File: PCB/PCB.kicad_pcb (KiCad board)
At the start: 2 copper layers, 64.8 x 61 mm, 54 parts, among them J2 Conn_01x02_Pin, J3 Conn_01x02_Pin, J5 Conn_01x04_Pin, SW1 SW_Push, U1 STM32L476RGTx, U2 FGPMMOPA6H, U4 TPS63001DRCR, U5 LM2735XMF/NOPB, U8 LM386, U9 MAX7375AXR805

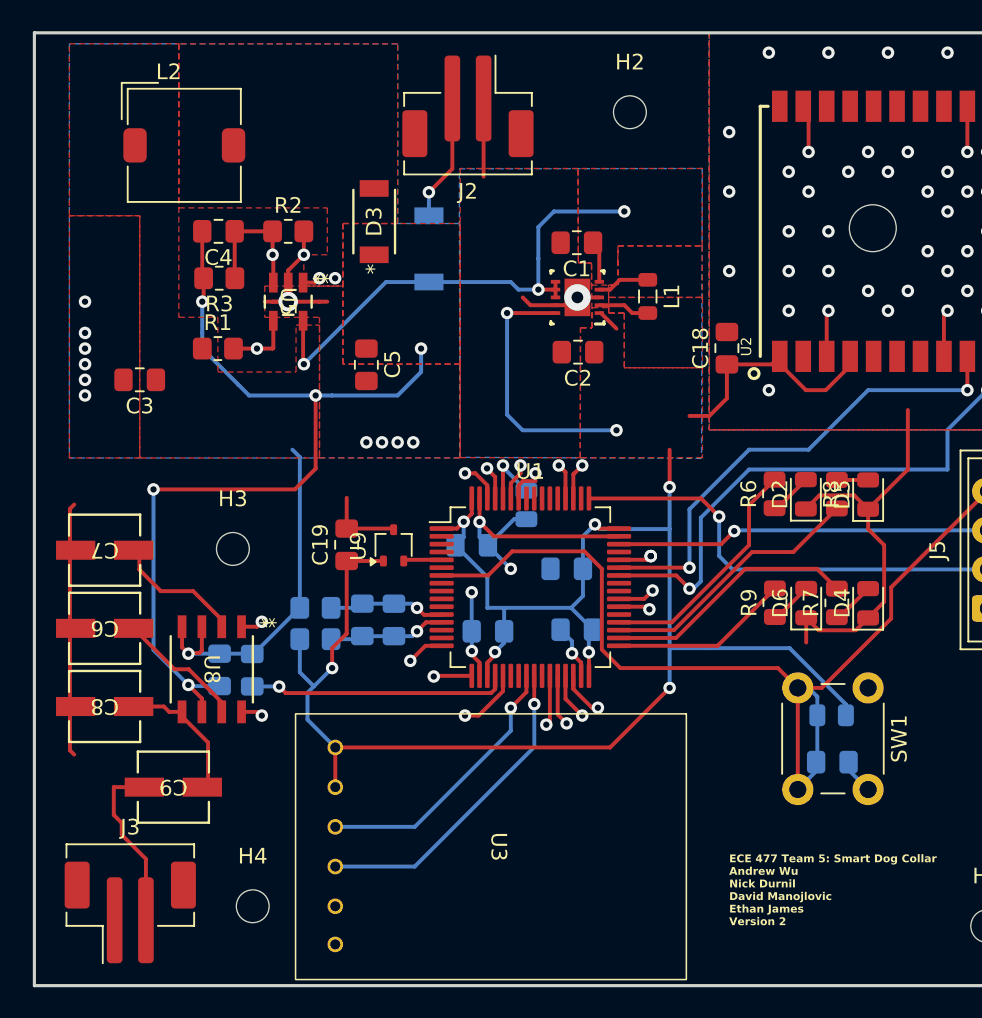
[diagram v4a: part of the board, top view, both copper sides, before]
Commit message: silkscreen visibility fix
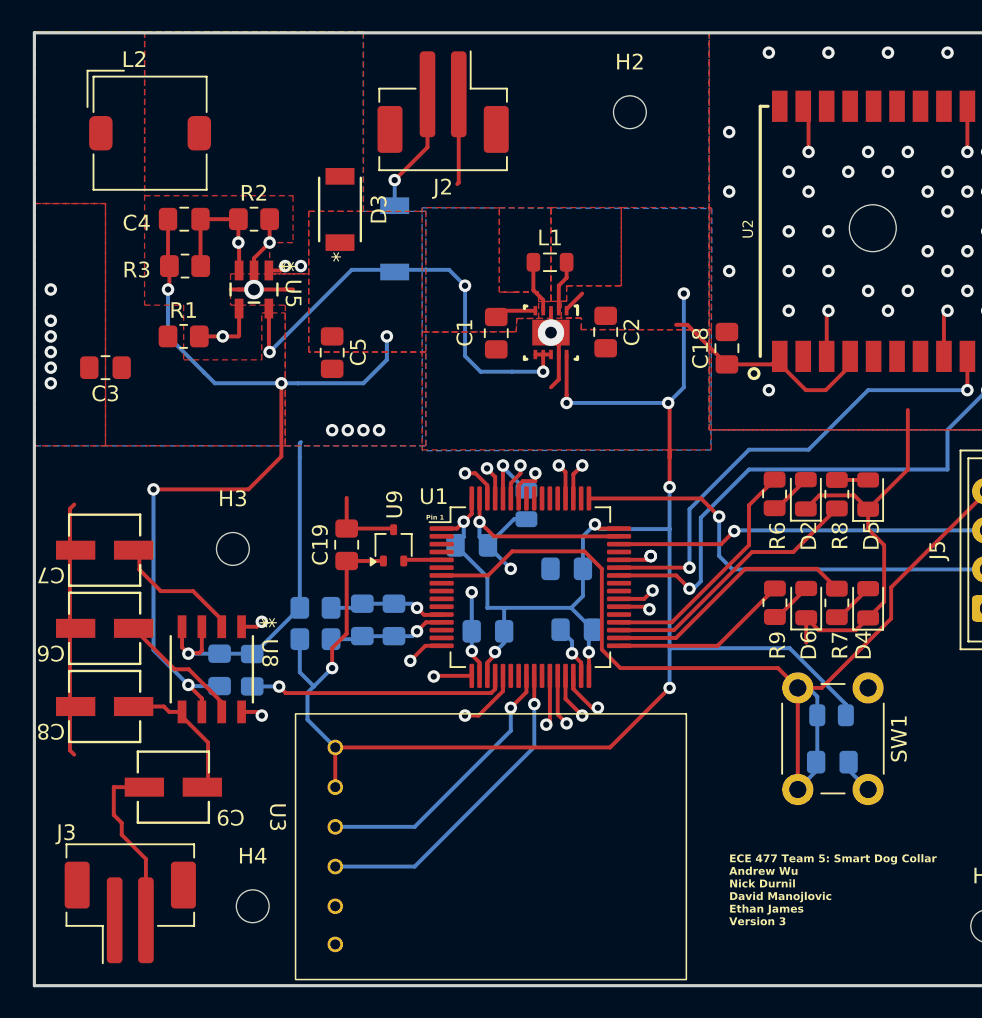
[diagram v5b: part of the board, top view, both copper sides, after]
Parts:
- moved C1 7.75 mm to (201.0, 103.0), turned to -90 degrees
- moved L1 6.63 mm to (204.4, 98.5), turned to 0 degrees
- moved U4 2.82 mm to (204.5, 103.0), turned to -90 degrees
- moved C3 2.32 mm to (176.0, 105.2)
- moved C4 2.32 mm to (181.0, 95.7)
- moved C5 2.32 mm to (190.5, 104.3)
- moved D3 2.32 mm to (191.0, 95.1)
- moved L2 2.32 mm to (178.8, 90.2)
- moved R1 2.32 mm to (181.0, 103.2)
- moved R2 2.32 mm to (185.5, 95.7)
- moved R3 2.32 mm to (181.1, 98.7)
- moved U5 2.32 mm to (185.5, 100.2)
- moved D1 2.28 mm to (194.5, 97.0)
- moved C2 2.19 mm to (208.0, 103.0), turned to -90 degrees
- moved J2 1.61 mm to (197.6, 88.2)
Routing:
- net +3.3V: track 145.3 -> 148.1 mm, vias 9 -> 10
- net /Bat +: track 34.9 -> 32.6 mm
- net +5V: track 58.1 -> 56.2 mm
- net GND: track 132.9 -> 134.0 mm
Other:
- board text added: "ECE 477 Team 5: Smart Dog Collar Andrew Wu Nick Durnil David Manojlovic Ethan James Version 3"
- board text added: "Pin 1"
- board text removed: "ECE 477 Team 5: Smart Dog Collar Andrew Wu Nick Durnil David Manojlovic Ethan James Version 2"

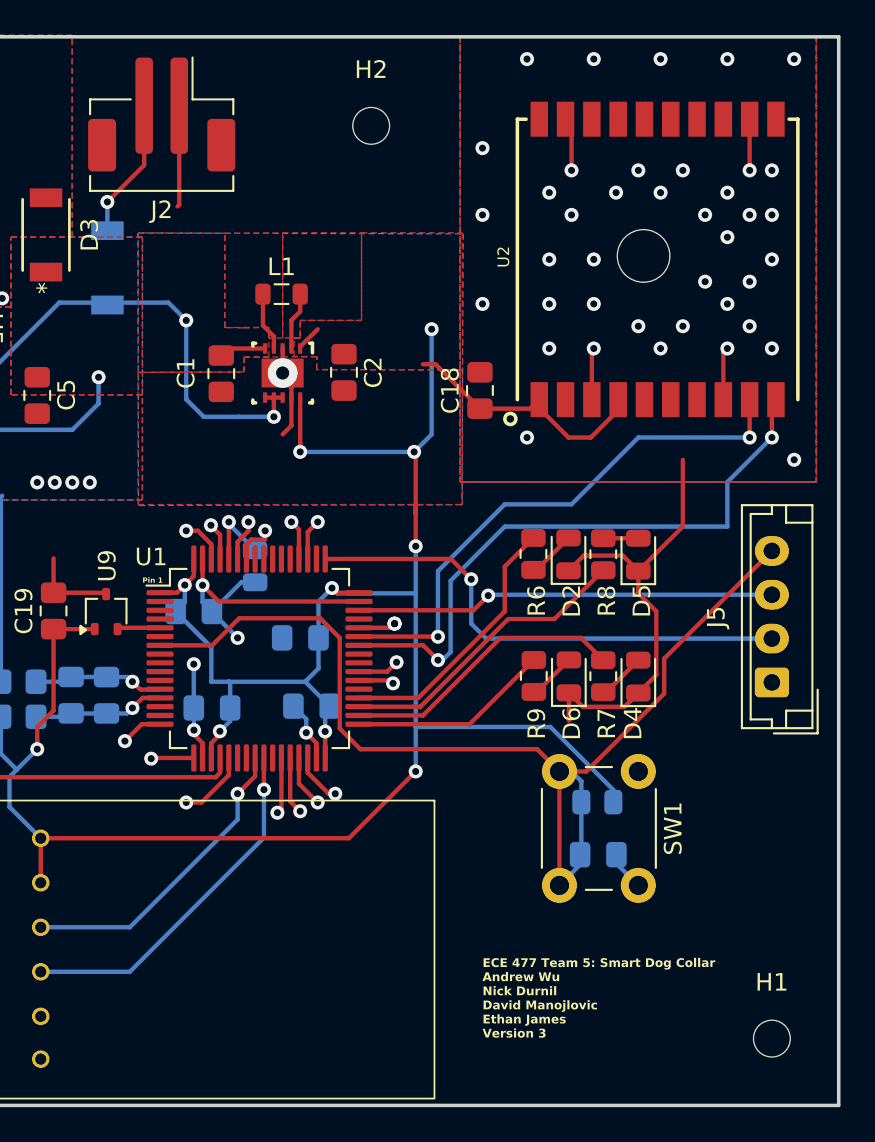
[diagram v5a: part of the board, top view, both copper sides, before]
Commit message: tweaks based on email
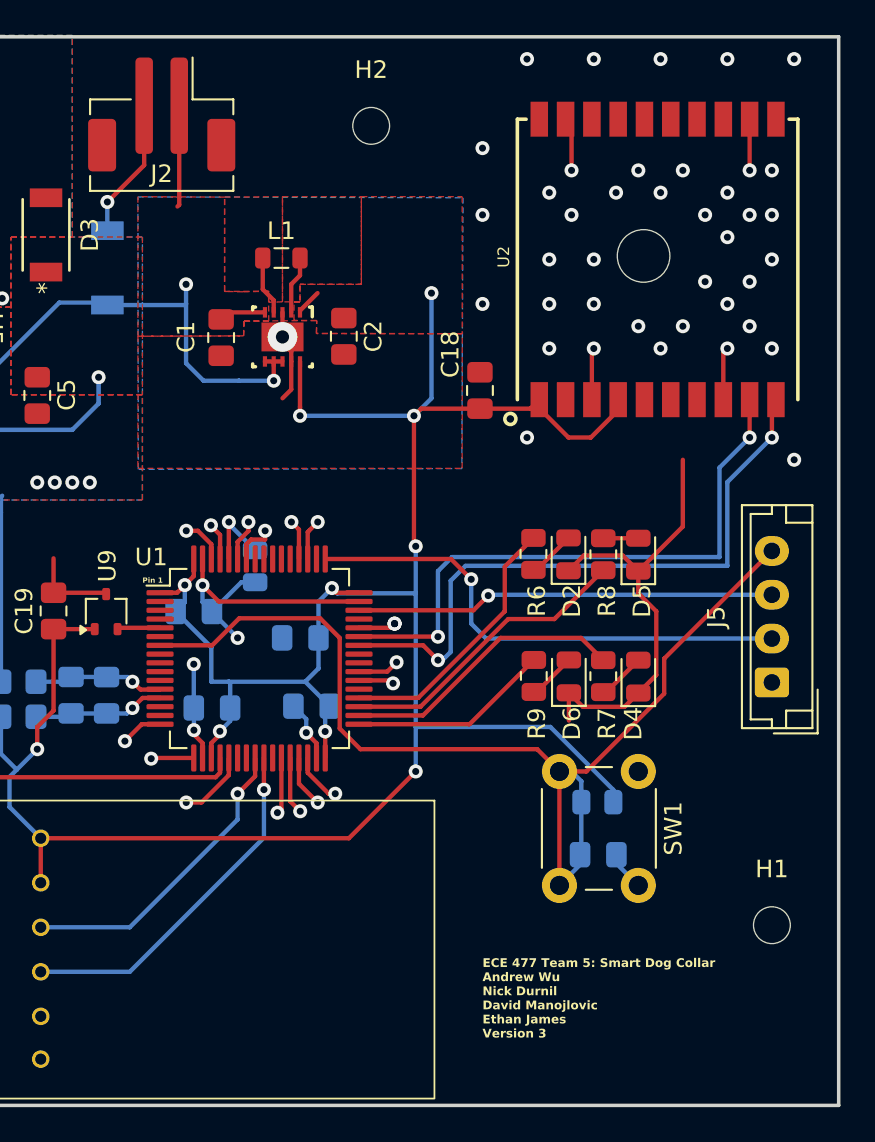
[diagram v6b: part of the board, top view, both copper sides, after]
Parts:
- moved H1 6.47 mm to (232.4, 134.5)
- moved C1 2.06 mm to (201.0, 101.0)
- moved C2 2.06 mm to (208.0, 100.9)
- moved L1 2.06 mm to (204.4, 96.4)
- moved U4 2.06 mm to (204.5, 100.9)
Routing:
- net /GPS TX: track 31.3 -> 34.3 mm
- net /GPS RX: track 35.3 -> 36.6 mm
- net +3.3V: track 148.1 -> 149.4 mm

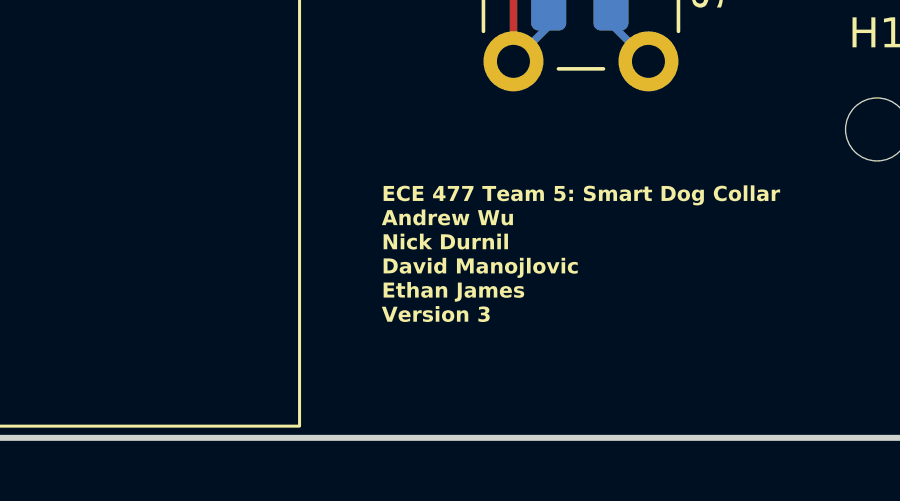
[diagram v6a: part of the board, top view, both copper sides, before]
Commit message: version change on silk screan
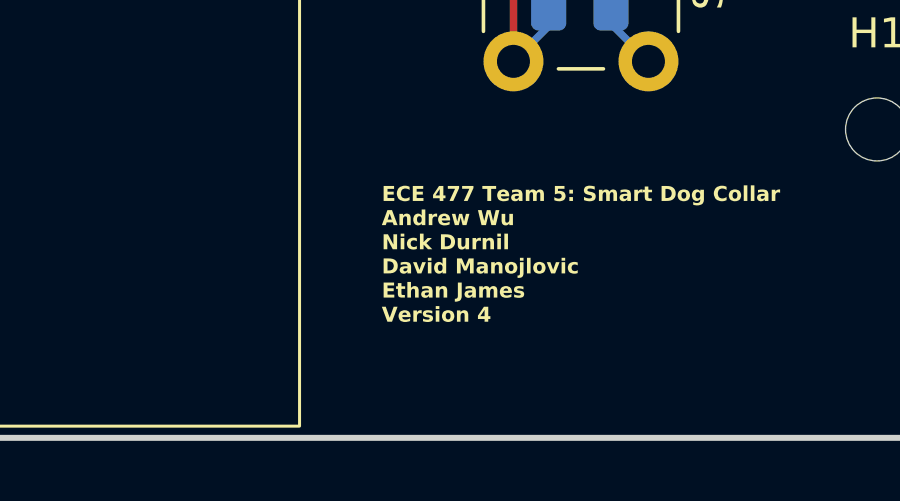
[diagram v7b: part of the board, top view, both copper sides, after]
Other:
- board text added: "ECE 477 Team 5: Smart Dog Collar Andrew Wu Nick Durnil David Manojlovic Ethan James Version 4"
- board text removed: "ECE 477 Team 5: Smart Dog Collar Andrew Wu Nick Durnil David Manojlovic Ethan James Version 3"
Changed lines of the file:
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@@
 		(layer "Edge.Cuts")
 	)
-	(gr_text "ECE 477 Team 5: Smart Dog Collar\nAndrew Wu\nNick Durnil\nDavid Manojlovic\nEthan James\nVersion 3"
+	(gr_text "ECE 477 Team 5: Smart Dog Collar\nAndrew Wu\nNick Durnil\nDavid Manojlovic\nEthan James\nVersion 4"
 		(at 215.9 140.97 0)
 		(layer "F.SilkS")

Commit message: pcb v5
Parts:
- moved H3 29.0 mm to (188.0, 88.1)
- moved H1 6.60 mm to (232.7, 127.9)
- moved U4 0.07 mm to (204.5, 100.9)
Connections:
- C11 pad 2: GND -> /Amp In
- U8 pad 3: GND -> /Amp In
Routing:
- net GND: track 134.0 -> 125.5 mm
- net /Amp In: track 0.00 -> 7.72 mm, vias 0 -> 1
- net /Bat +: track 32.2 -> 35.8 mm
- net /TIM 4 CH 3: track 2.27 -> 3.93 mm
- net /UART TX: track 2.35 -> 3.94 mm
- net /UART RX: track 2.29 -> 3.82 mm
- net /TIM 4 CH 4: track 2.59 -> 3.88 mm
- net /TIM 4 CH 2: track 2.37 -> 3.53 mm
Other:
- board text added: "*"
- board text added: "ECE 477 Team 5: Smart Dog Collar Andrew Wu Nick Durnil David Manojlovic Ethan James Version 5"
- board text removed: "ECE 477 Team 5: Smart Dog Collar Andrew Wu Nick Durnil David Manojlovic Ethan James Version 4"
- board text removed: "Pin 1"
